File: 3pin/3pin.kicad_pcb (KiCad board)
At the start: 2 copper layers, 10 x 20 mm, 2 parts, among them J1 B03B-PASK-1(LF)(SN), J2 Conn_01x03

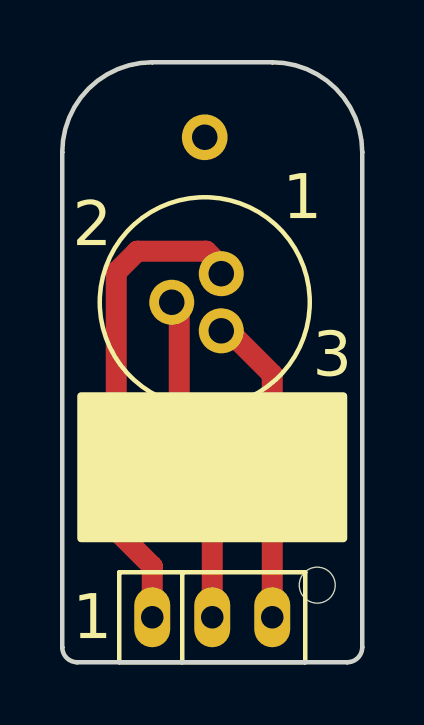
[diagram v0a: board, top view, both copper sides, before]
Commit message: Modif of gerber file for the pin 3 fischer
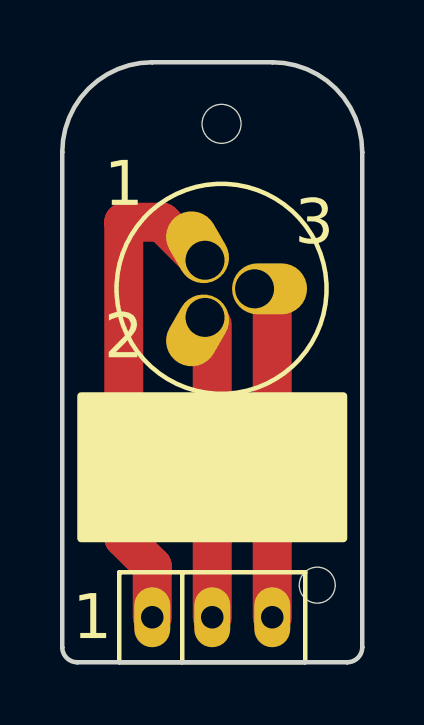
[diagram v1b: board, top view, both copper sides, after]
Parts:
- moved J2 0.72 mm to (149.3, 102.6)
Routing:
- net Net-(J1-Pad3): track 10.1 -> 11.4 mm
- net Net-(J1-Pad2): track 11.0 -> 10.1 mm
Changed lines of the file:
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@@
-(kicad_pcb (version 4) (host pcbnew 4.0.7-e2-6376~58~ubuntu16.04.1)
+(kicad_pcb (version 20171130) (host pcbnew "(5.0.2)-1")
   (general
-    (links 3)
-    (no_connects 0)
-    (area 137.857144 94.924999 165.85 119.200001)
     (thickness 1.6)
     (drawings 14)
@@
     (mod_text_size 1 1)
     (mod_text_width 0.15)
-    (pad_size 1.524 1.524)
-    (pad_drill 0.762)
+    (pad_size 1.3 1.3)
+    (pad_drill 1.3)
     (pad_to_mask_clearance 0.2)
+    (solder_mask_min_width 0.25)
     (aux_axis_origin 0 0)
-    (visible_elements FFFFFF7F)
+    (visible_elements 7FFFFFFF)
     (pcbplotparams
       (layerselection 0x010f0_80000001)
       (usegerberextensions true)
+      (usegerberattributes false)
+      (usegerberadvancedattributes false)
+      (creategerberjobfile false)
       (excludeedgelayer true)
       (linewidth 0.100000)
@@
       (hpglpennumber 1)
       (hpglpenspeed 20)
-      (hpglpendiameter 15)
-      (hpglpenoverlay 2)
+      (hpglpendiameter 15.000000)
       (psnegative false)
       (psa4output false)
@@
       (drillshape 0)
       (scaleselection 1)
-      (outputdirectory ../fabrication/3pin/))
+      (outputdirectory "../fabrication/3pin/"))
   )
   (net 0 "")
@@
     (add_net "Net-(J1-Pad2)")
     (add_net "Net-(J1-Pad3)")
+  )
+  (module fihser:UR07-3 (layer F.Cu)
+    (at 149.310001 102.552627)
+    (fp_text reference J2 (at -2.78 0 90) (layer F.SilkS) hide
+      (effects (font (size 1.2 1.2) (thickness 0.15)))
+    )
+    (fp_text value Conn_01x03 (at 0 2.825) (layer F.Fab) hide
+      (effects (font (size 1.2 1.2) (thickness 0.15)))
+    )
+    (fp_circle (center 0 0) (end 0 3.5) (layer F.SilkS) (width 0.15))
+    (fp_circle (center 0 0) (end 7.5 0) (layer F.CrtYd) (width 0.15))
+    (pad "" np_thru_hole circle (at 0 -5.5 90) (size 1.3 1.3) (drill 1.3) (layers *.Cu *.Mask))
+    (pad 2 thru_hole oval (at -0.55 0.952627 60) (size 2.5 1.7) (drill 1.3 (offset -0.5 0)) (layers *.Cu *.Mask)
+      (net 2 "Net-(J1-Pad2)"))
+    (pad 3 thru_hole oval (at 1.1 0) (size 2.5 1.7) (drill 1.3 (offset 0.5 0)) (layers *.Cu *.Mask)
+      (net 3 "Net-(J1-Pad3)"))
+    (pad 1 thru_hole oval (at -0.55 -0.952627 300) (size 2.5 1.7) (drill 1.3 (offset -0.5 0)) (layers *.Cu *.Mask)
+      (net 1 "Net-(J1-Pad1)"))
   )
   (module "jstpa:B03B-PASK-1(LF)(SN)" (layer F.Cu)
@@
       (net 3 "Net-(J1-Pad3)"))
     (pad "" np_thru_hole circle (at 3.5 -1.07) (size 1.2 1.2) (drill 1.2) (layers *.Cu *.Mask))
-  )
-  (module fihser:UR07-3 (layer F.Cu)
-    (at 148.75 103)
-    (fp_text reference J2 (at -2.78 0 90) (layer F.SilkS) hide
-      (effects (font (size 1.2 1.2) (thickness 0.15)))
-    )
-    (fp_text value Conn_01x03 (at 0 2.825) (layer F.Fab) hide
-      (effects (font (size 1.2 1.2) (thickness 0.15)))
-    )
-    (fp_circle (center 0 0) (end 7.5 0) (layer F.CrtYd) (width 0.15))
-    (fp_circle (center 0 0) (end 0 3.5) (layer F.SilkS) (width 0.15))
-    (pad 1 thru_hole oval (at 0.549999 -0.952627) (size 1.5 1.5) (drill 0.85) (layers *.Cu *.Mask)
-      (net 1 "Net-(J1-Pad1)"))
-    (pad 2 thru_hole oval (at -1.1 0) (size 1.5 1.5) (drill 0.85) (layers *.Cu *.Mask)
-      (net 2 "Net-(J1-Pad2)"))
-    (pad 3 thru_hole oval (at 0.55 0.952627) (size 1.5 1.5) (drill 0.85) (layers *.Cu *.Mask)
-      (net 3 "Net-(J1-Pad3)"))
-    (pad "" thru_hole circle (at 0 -5.5 90) (size 1.524 1.524) (drill 0.85) (layers *.Cu *.Mask))
   )
   (dimension 10 (width 0.3) (layer Cmts.User)
@@
     (arrow2b (pts (xy 158 95) (xy 158.586421 96.126504)))
   )
-  (gr_text 3 (at 153 104.75) (layer F.SilkS)
+  (gr_text 3 (at 152.4 100.33) (layer F.SilkS)
     (effects (font (size 1.5 1.5) (thickness 0.3)))
   )
-  (gr_text 2 (at 145 100.4) (layer F.SilkS)
+  (gr_text 2 (at 146.05 104.14) (layer F.SilkS)
     (effects (font (size 1.5 1.5) (thickness 0.3)))
   )
-  (gr_text 1 (at 152 99.5) (layer F.SilkS)
+  (gr_text 1 (at 146.05 99.06) (layer F.SilkS)
     (effects (font (size 1.5 1.5) (thickness 0.3)))
   )
@@
   (gr_line (start 154 114.5) (end 154 98) (layer Edge.Cuts) (width 0.15))
   (gr_line (start 144.5 115) (end 153.5 115) (layer Edge.Cuts) (width 0.15))
-  (segment (start 149.549999 102.047373) (end 148.8 101.297374) (width 0.7) (layer F.Cu) (net 1))
-  (segment (start 148.8 101.297374) (end 146.502626 101.297374) (width 0.7) (layer F.Cu) (net 1))
-  (segment (start 146.502626 101.297374) (end 145.8 102) (width 0.7) (layer F.Cu) (net 1))
-  (segment (start 145.8 102) (end 145.8 110.6) (width 0.7) (layer F.Cu) (net 1))
-  (segment (start 145.8 110.6) (end 147 111.8) (width 0.7) (layer F.Cu) (net 1))
-  (segment (start 147 111.8) (end 147 113.5) (width 0.7) (layer F.Cu) (net 1))
-  (segment (start 149 107.6) (end 147.9 106.5) (width 0.7) (layer F.Cu) (net 2))
-  (segment (start 147.9 106.5) (end 147.9 103) (width 0.7) (layer F.Cu) (net 2))
-  (segment (start 149 113.5) (end 149 107.6) (width 0.7) (layer F.Cu) (net 2))
-  (segment (start 151 113.5) (end 151 105.402627) (width 0.7) (layer F.Cu) (net 3))
-  (segment (start 151 105.402627) (end 149.55 103.952627) (width 0.7) (layer F.Cu) (net 3))
+  (segment (start 148.760001 101.6) (end 148.59 101.6) (width 0.7) (layer F.Cu) (net 1))
+  (segment (start 148.59 101.6) (end 147.32 100.33) (width 1.3) (layer F.Cu) (net 1))
+  (segment (start 147.32 100.33) (end 146.05 100.33) (width 1.3) (layer F.Cu) (net 1))
+  (segment (start 147 111.8) (end 147 113.5) (width 1.3) (layer F.Cu) (net 1))
+  (segment (start 146.05 110.85) (end 147 111.8) (width 1.3) (layer F.Cu) (net 1))
+  (segment (start 146.05 100.33) (end 146.05 110.85) (width 1.3) (layer F.Cu) (net 1))
+  (segment (start 149 103.745253) (end 149 113.5) (width 1.3) (layer F.Cu) (net 2))
+  (segment (start 148.760001 103.505254) (end 149 103.745253) (width 0.7) (layer F.Cu) (net 2))
+  (segment (start 150.410001 102.552627) (end 150.812627 102.552627) (width 0.7) (layer F.Cu) (net 3))
+  (segment (start 151 102.74) (end 151 113.5) (width 1.3) (layer F.Cu) (net 3))
+  (segment (start 150.812627 102.552627) (end 151 102.74) (width 0.7) (layer F.Cu) (net 3))
   (zone (net 0) (net_name "") (layer F.SilkS) (hatch edge 0.508)
     (connect_pads (clearance 0.508))

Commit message: Change design and foot print of the 5 pin, fabrication 3 pins near done
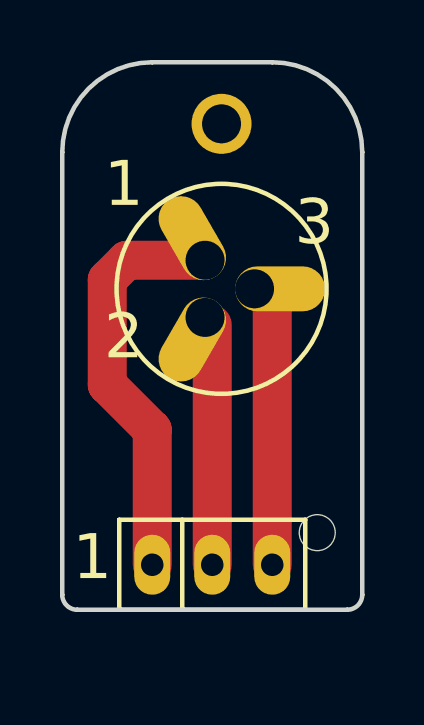
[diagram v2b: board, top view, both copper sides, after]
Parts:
- moved J1 1.75 mm to (149.0, 111.8)
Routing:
- net Net-(J1-Pad1): track 16.8 -> 13.8 mm
- net Net-(J1-Pad2): track 10.1 -> 8.34 mm
- net Net-(J1-Pad3): track 11.4 -> 10.2 mm
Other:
- board size 10 x 20 mm -> 10 x 18.2 mm
- net class Default: trace_width 0.7 -> 1.3
- rule pad_to_mask_clearance: 0.2 -> 0.1
- rule solder_mask_min_width: 0.25 -> 0.1
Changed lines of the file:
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@@
     (thickness 1.6)
     (drawings 14)
-    (tracks 11)
+    (tracks 13)
     (zones 0)
     (modules 2)
@@
   )
   (setup
-    (last_trace_width 0.7)
+    (last_trace_width 1.3)
     (trace_clearance 0.2)
     (zone_clearance 0.508)
@@
     (pad_size 1.3 1.3)
     (pad_drill 1.3)
-    (pad_to_mask_clearance 0.2)
-    (solder_mask_min_width 0.25)
+    (pad_to_mask_clearance 0.1)
+    (solder_mask_min_width 0.1)
     (aux_axis_origin 0 0)
     (visible_elements 7FFFFFFF)
     (pcbplotparams
-      (layerselection 0x010f0_80000001)
+      (layerselection 0x01000_7fffffff)
       (usegerberextensions true)
       (usegerberattributes false)
@@
   (net_class Default "This is the default net class."
     (clearance 0.2)
-    (trace_width 0.7)
+    (trace_width 1.3)
     (via_dia 0.6)
     (via_drill 0.4)
@@
     (fp_circle (center 0 0) (end 0 3.5) (layer F.SilkS) (width 0.15))
     (fp_circle (center 0 0) (end 7.5 0) (layer F.CrtYd) (width 0.15))
-    (pad "" np_thru_hole circle (at 0 -5.5 90) (size 1.3 1.3) (drill 1.3) (layers *.Cu *.Mask))
-    (pad 2 thru_hole oval (at -0.55 0.952627 60) (size 2.5 1.7) (drill 1.3 (offset -0.5 0)) (layers *.Cu *.Mask)
+    (pad "" thru_hole circle (at 0 -5.5 90) (size 2 2) (drill 1.3) (layers *.Cu *.Mask))
+    (pad 2 thru_hole oval (at -0.55 0.952627 60) (size 3 1.5) (drill 1.3 (offset -0.85 0)) (layers *.Cu *.Mask)
       (net 2 "Net-(J1-Pad2)"))
-    (pad 3 thru_hole oval (at 1.1 0) (size 2.5 1.7) (drill 1.3 (offset 0.5 0)) (layers *.Cu *.Mask)
+    (pad 3 thru_hole oval (at 1.1 0) (size 3 1.5) (drill 1.3 (offset 0.85 0)) (layers *.Cu *.Mask)
       (net 3 "Net-(J1-Pad3)"))
-    (pad 1 thru_hole oval (at -0.55 -0.952627 300) (size 2.5 1.7) (drill 1.3 (offset -0.5 0)) (layers *.Cu *.Mask)
+    (pad 1 thru_hole oval (at -0.55 -0.952627 300) (size 3 1.5) (drill 1.3 (offset -0.85 0)) (layers *.Cu *.Mask)
       (net 1 "Net-(J1-Pad1)"))
   )
   (module "jstpa:B03B-PASK-1(LF)(SN)" (layer F.Cu)
-    (at 149 113.5)
+    (at 149 111.75)
     (fp_text reference J1 (at -4 0 90) (layer F.SilkS) hide
       (effects (font (size 1.2 1.2) (thickness 0.15)))
@@
       (effects (font (size 1.2 1.2) (thickness 0.15)))
     )
+    (fp_line (start -1 -1.5) (end -1 1.5) (layer F.SilkS) (width 0.15))
+    (fp_line (start -3.1 1.5) (end -3.1 -1.5) (layer F.SilkS) (width 0.15))
+    (fp_line (start 3.1 1.5) (end -3.1 1.5) (layer F.SilkS) (width 0.15))
+    (fp_line (start 3.1 -1.5) (end 3.1 1.5) (layer F.SilkS) (width 0.15))
     (fp_line (start -3.1 -1.5) (end 3.1 -1.5) (layer F.SilkS) (width 0.15))
-    (fp_line (start 3.1 -1.5) (end 3.1 1.5) (layer F.SilkS) (width 0.15))
-    (fp_line (start 3.1 1.5) (end -3.1 1.5) (layer F.SilkS) (width 0.15))
-    (fp_line (start -3.1 1.5) (end -3.1 -1.5) (layer F.SilkS) (width 0.15))
-    (fp_line (start -1 -1.5) (end -1 1.5) (layer F.SilkS) (width 0.15))
+    (pad "" np_thru_hole circle (at 3.5 -1.07) (size 1.2 1.2) (drill 1.2) (layers *.Cu *.Mask))
+    (pad 3 thru_hole oval (at 2 0) (size 1.2 2) (drill 0.75) (layers *.Cu *.Mask)
+      (net 3 "Net-(J1-Pad3)"))
+    (pad 2 thru_hole oval (at 0 0) (size 1.2 2) (drill 0.75) (layers *.Cu *.Mask)
+      (net 2 "Net-(J1-Pad2)"))
     (pad 1 thru_hole oval (at -2 0) (size 1.2 2) (drill 0.75) (layers *.Cu *.Mask)
       (net 1 "Net-(J1-Pad1)"))
-    (pad 2 thru_hole oval (at 0 0) (size 1.2 2) (drill 0.75) (layers *.Cu *.Mask)
-      (net 2 "Net-(J1-Pad2)"))
-    (pad 3 thru_hole oval (at 2 0) (size 1.2 2) (drill 0.75) (layers *.Cu *.Mask)
-      (net 3 "Net-(J1-Pad3)"))
-    (pad "" np_thru_hole circle (at 3.5 -1.07) (size 1.2 1.2) (drill 1.2) (layers *.Cu *.Mask))
   )
   (dimension 10 (width 0.3) (layer Cmts.User)
-    (gr_text "10.000 mm" (at 149 117.85) (layer Cmts.User)
+    (gr_text "10.000 mm" (at 149 119.85) (layer Cmts.User)
       (effects (font (size 1.5 1.5) (thickness 0.3)))
     )
-    (feature1 (pts (xy 154 105) (xy 154 119.2)))
-    (feature2 (pts (xy 144 105) (xy 144 119.2)))
-    (crossbar (pts (xy 144 116.5) (xy 154 116.5)))
-    (arrow1a (pts (xy 154 116.5) (xy 152.873496 117.086421)))
-    (arrow1b (pts (xy 154 116.5) (xy 152.873496 115.913579)))
-    (arrow2a (pts (xy 144 116.5) (xy 145.126504 117.086421)))
-    (arrow2b (pts (xy 144 116.5) (xy 145.126504 115.913579)))
+    (feature1 (pts (xy 154 105) (xy 154 118.336421)))
+    (feature2 (pts (xy 144 105) (xy 144 118.336421)))
+    (crossbar (pts (xy 144 117.75) (xy 154 117.75)))
+    (arrow1a (pts (xy 154 117.75) (xy 152.873496 118.336421)))
+    (arrow1b (pts (xy 154 117.75) (xy 152.873496 117.163579)))
+    (arrow2a (pts (xy 144 117.75) (xy 145.126504 118.336421)))
+    (arrow2b (pts (xy 144 117.75) (xy 145.126504 117.163579)))
   )
-  (dimension 20 (width 0.3) (layer Cmts.User)
-    (gr_text "20.000 mm" (at 159.35 105 270) (layer Cmts.User)
+  (dimension 18.25 (width 0.3) (layer Cmts.User)
+    (gr_text "18.250 mm" (at 160.1 104.125 270) (layer Cmts.User)
       (effects (font (size 1.5 1.5) (thickness 0.3)))
     )
-    (feature1 (pts (xy 149 115) (xy 160.7 115)))
-    (feature2 (pts (xy 149 95) (xy 160.7 95)))
-    (crossbar (pts (xy 158 95) (xy 158 115)))
-    (arrow1a (pts (xy 158 115) (xy 157.413579 113.873496)))
-    (arrow1b (pts (xy 158 115) (xy 158.586421 113.873496)))
+    (feature1 (pts (xy 149 113.25) (xy 158.586421 113.25)))
+    (feature2 (pts (xy 149 95) (xy 158.586421 95)))
+    (crossbar (pts (xy 158 95) (xy 158 113.25)))
+    (arrow1a (pts (xy 158 113.25) (xy 157.413579 112.123496)))
+    (arrow1b (pts (xy 158 113.25) (xy 158.586421 112.123496)))
     (arrow2a (pts (xy 158 95) (xy 157.413579 96.126504)))
     (arrow2b (pts (xy 158 95) (xy 158.586421 96.126504)))
@@
     (effects (font (size 1.5 1.5) (thickness 0.3)))
   )
-  (gr_text 1 (at 145 113.5) (layer F.SilkS)
+  (gr_text 1 (at 145 111.5) (layer F.SilkS)
     (effects (font (size 1.5 1.5) (thickness 0.3)))
   )
   (gr_arc (start 151 98) (end 151 95) (angle 90) (layer Edge.Cuts) (width 0.15))
   (gr_arc (start 147 98) (end 144 98) (angle 90) (layer Edge.Cuts) (width 0.15))
-  (gr_arc (start 144.5 114.5) (end 144.5 115) (angle 90) (layer Edge.Cuts) (width 0.15))
-  (gr_arc (start 153.5 114.5) (end 154 114.5) (angle 90) (layer Edge.Cuts) (width 0.15))
-  (gr_line (start 144 98) (end 144 114.5) (layer Edge.Cuts) (width 0.15))
+  (gr_arc (start 144.5 112.75) (end 144.5 113.25) (angle 90) (layer Edge.Cuts) (width 0.15))
+  (gr_arc (start 153.5 112.75) (end 154 112.75) (angle 90) (layer Edge.Cuts) (width 0.15))
+  (gr_line (start 144 98) (end 144 112.75) (layer Edge.Cuts) (width 0.15))
   (gr_line (start 151 95) (end 147 95) (layer Edge.Cuts) (width 0.15))
-  (gr_line (start 154 114.5) (end 154 98) (layer Edge.Cuts) (width 0.15))
-  (gr_line (start 144.5 115) (end 153.5 115) (layer Edge.Cuts) (width 0.15))
+  (gr_line (start 154 112.75) (end 154 98) (layer Edge.Cuts) (width 0.15))
+  (gr_line (start 144.5 113.25) (end 153.5 113.25) (layer Edge.Cuts) (width 0.15))
   (segment (start 148.760001 101.6) (end 148.59 101.6) (width 0.7) (layer F.Cu) (net 1))
-  (segment (start 148.59 101.6) (end 147.32 100.33) (width 1.3) (layer F.Cu) (net 1))
-  (segment (start 147.32 100.33) (end 146.05 100.33) (width 1.3) (layer F.Cu) (net 1))
-  (segment (start 147 111.8) (end 147 113.5) (width 1.3) (layer F.Cu) (net 1))
-  (segment (start 146.05 110.85) (end 147 111.8) (width 1.3) (layer F.Cu) (net 1))
-  (segment (start 146.05 100.33) (end 146.05 110.85) (width 1.3) (layer F.Cu) (net 1))
-  (segment (start 149 103.745253) (end 149 113.5) (width 1.3) (layer F.Cu) (net 2))
+  (segment (start 146.15 101.6) (end 148.760001 101.6) (width 1.3) (layer F.Cu) (net 1))
+  (segment (start 145.5 102.25) (end 146.15 101.6) (width 1.3) (layer F.Cu) (net 1))
+  (segment (start 145.5 105.75) (end 145.5 102.25) (width 1.3) (layer F.Cu) (net 1))
+  (segment (start 147 111.75) (end 147 107.25) (width 1.3) (layer F.Cu) (net 1))
+  (segment (start 147 107.25) (end 145.5 105.75) (width 1.3) (layer F.Cu) (net 1))
+  (segment (start 149 103.745253) (end 149 111.75) (width 1.3) (layer F.Cu) (net 2))
   (segment (start 148.760001 103.505254) (end 149 103.745253) (width 0.7) (layer F.Cu) (net 2))
   (segment (start 150.410001 102.552627) (end 150.812627 102.552627) (width 0.7) (layer F.Cu) (net 3))
-  (segment (start 151 102.74) (end 151 113.5) (width 1.3) (layer F.Cu) (net 3))
   (segment (start 150.812627 102.552627) (end 151 102.74) (width 0.7) (layer F.Cu) (net 3))
-  (zone (net 0) (net_name "") (layer F.SilkS) (hatch edge 0.508)
-    (connect_pads (clearance 0.508))
-    (min_thickness 0.254)
-    (fill yes (arc_segments 16) (thermal_gap 0.508) (thermal_bridge_width 0.508))
-    (polygon
-      (pts
-        (xy 144.5 106) (xy 153.5 106) (xy 153.5 111) (xy 144.5 111)
-      )
-    )
-  )
+  (segment (start 150.410001 102.552627) (end 150.552627 102.552627) (width 0.7) (layer F.Cu) (net 3))
+  (segment (start 151 103) (end 151 111.75) (width 1.3) (layer F.Cu) (net 3))
+  (segment (start 150.552627 102.552627) (end 151 103) (width 0.7) (layer F.Cu) (net 3))
 )
